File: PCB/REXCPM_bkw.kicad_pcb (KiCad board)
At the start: 2 copper layers, 38 x 16.6 mm, 19 parts, among them J1 Tandy_100_102_200_option_rom, J2 SM04B, U1 XCR3064XL, U2 RMLV3216AGSA, U3 4245, U4 4245, U5 NCV563SQ33, U6 NCV563SQ33

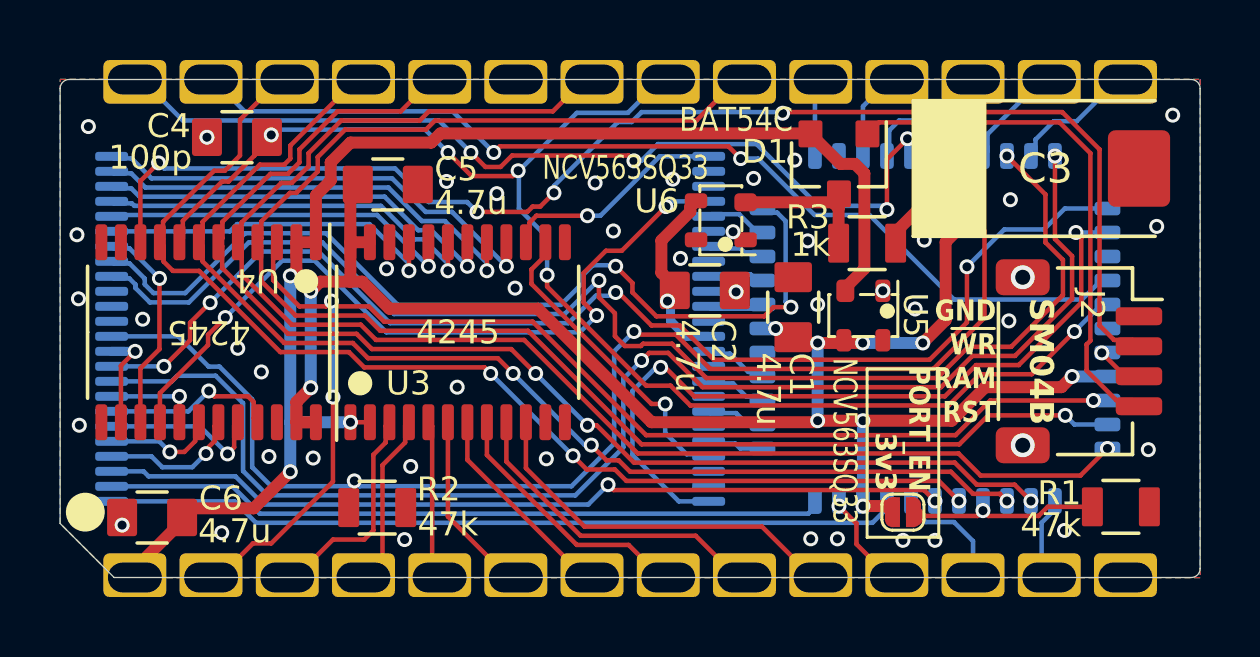
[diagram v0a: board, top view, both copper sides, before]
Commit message: housing component, fillet tracks, molex datasheets corrections
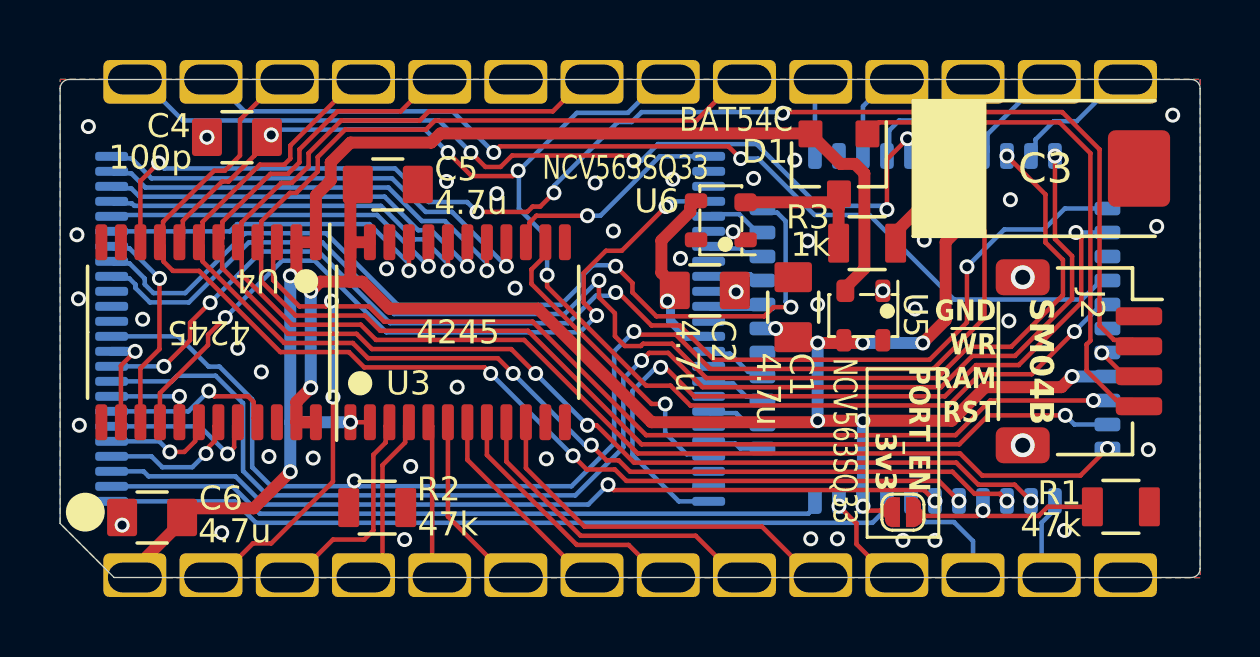
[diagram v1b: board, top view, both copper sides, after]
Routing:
- net +3V3: track 57.3 -> 58.0 mm
